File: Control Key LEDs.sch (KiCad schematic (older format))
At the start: 32 parts

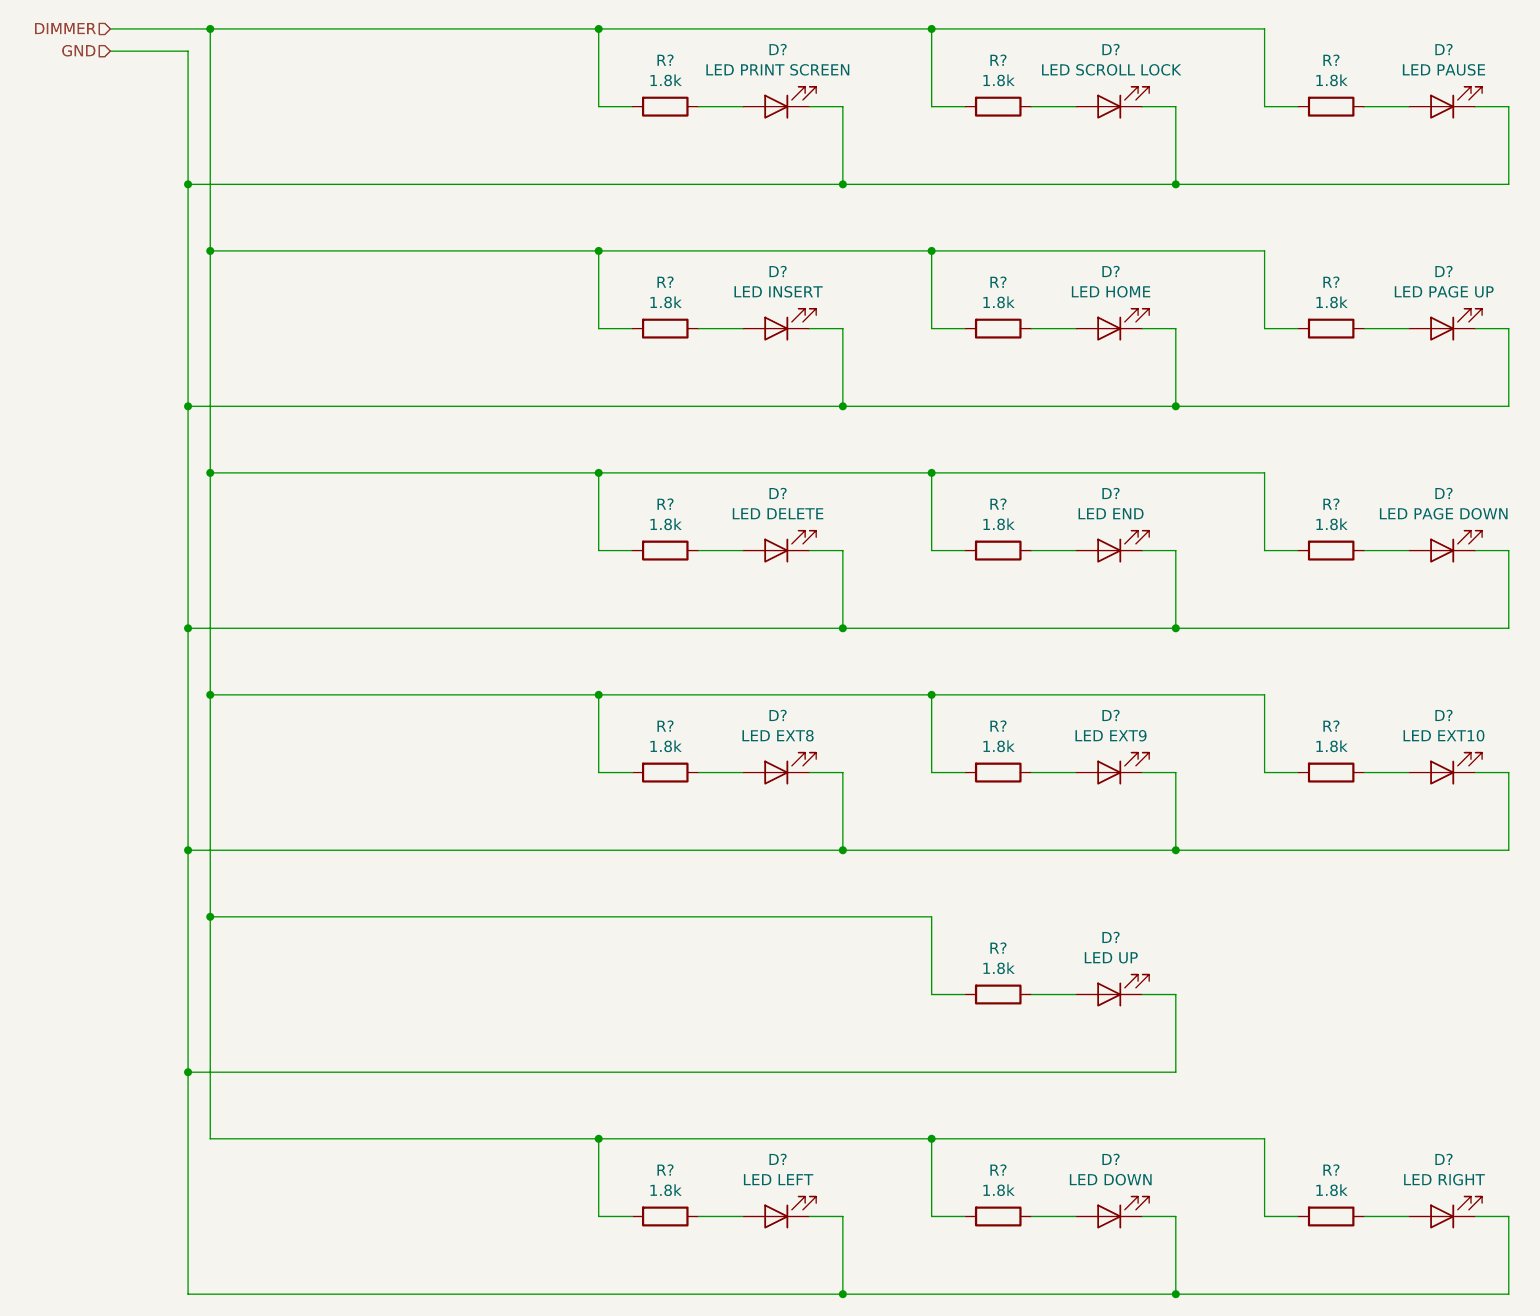
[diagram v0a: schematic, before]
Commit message: Corrected errors found in design rule check
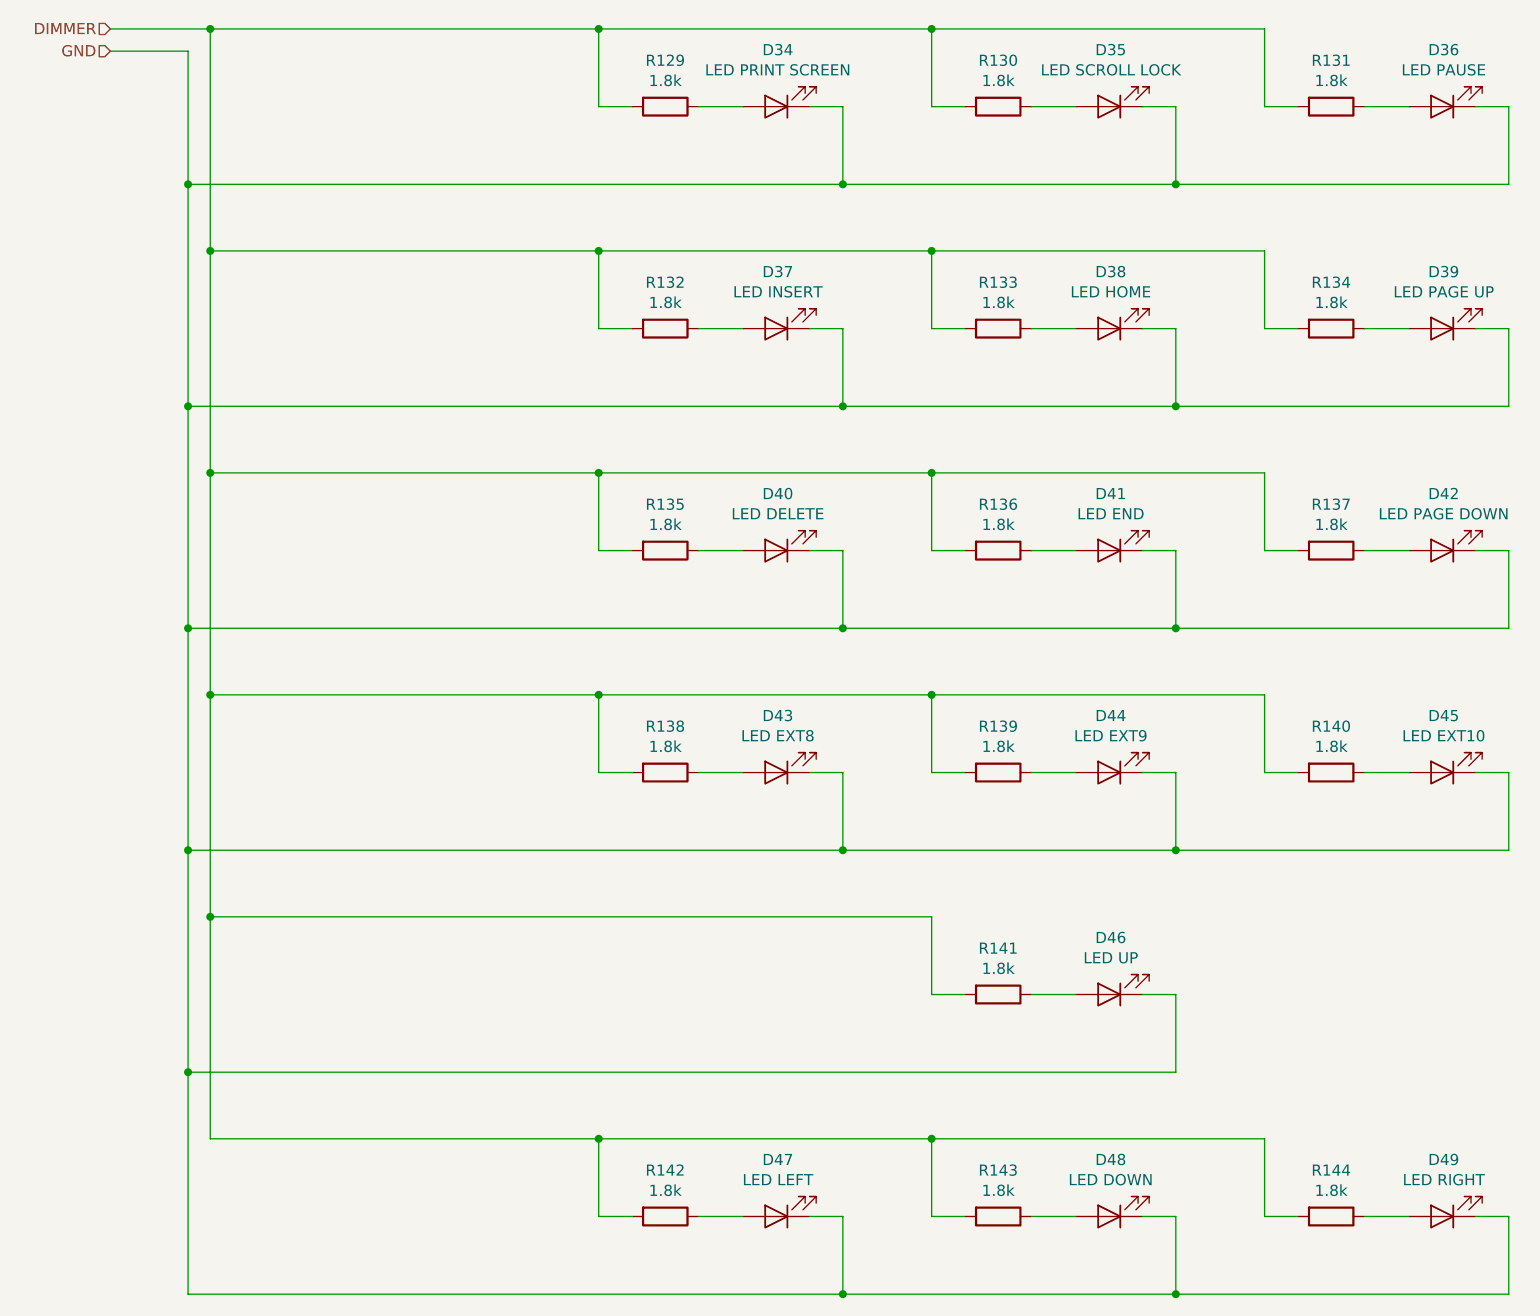
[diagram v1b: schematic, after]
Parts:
- D34, D35, D36, D37, D38, D39, D40, D41, D42, D43, D44, D45, D46, D47, D48, D49: renamed from D?; footprint (none) -> LED_SMD:LED_1206_3216Metric_ReverseMount_Hole1.8x2.4mm
- R129, R130, R131, R132, R133, R134, R135, R136, R137, R138, R139, R140, R141, R142, R143, R144: renamed from R?; footprint (none) -> Resistor_SMD:R_1206_3216Metric_Pad1.42x1.75mm_HandSolder

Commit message: Redesigned for single large PCB
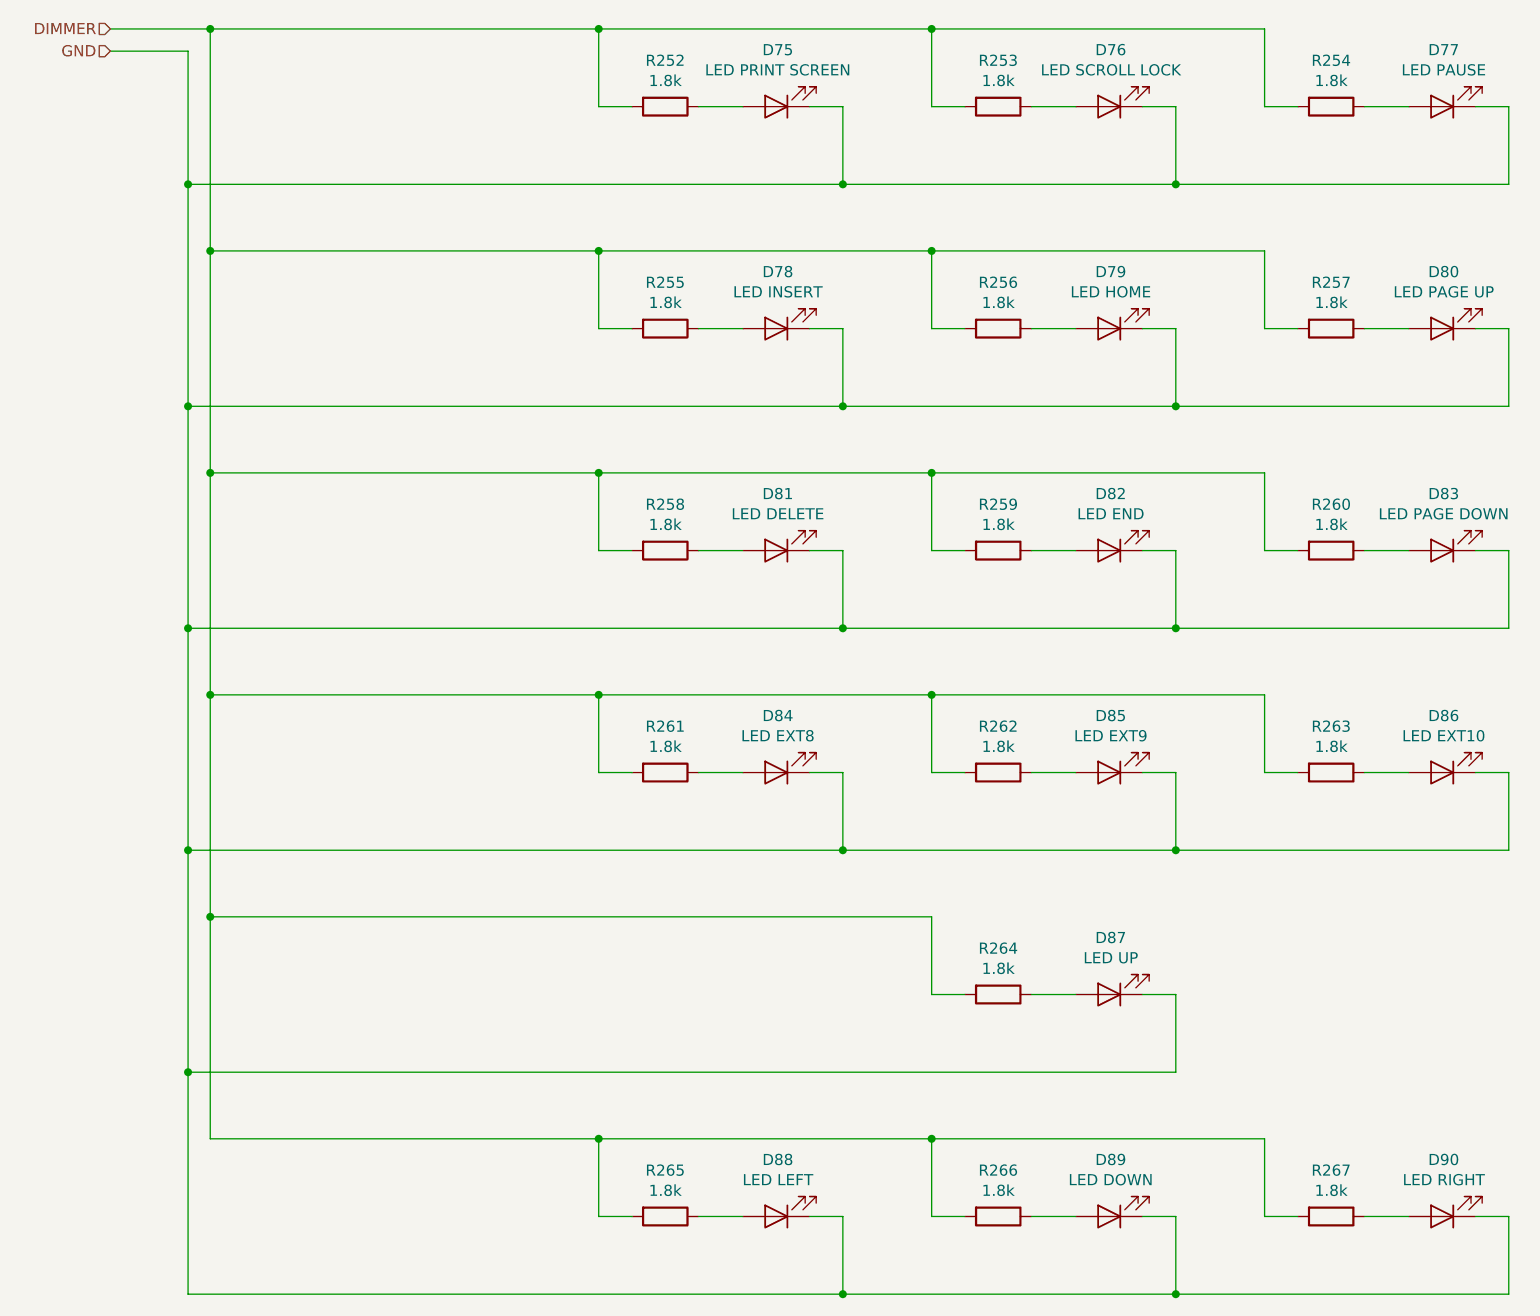
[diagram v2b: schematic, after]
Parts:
- renumbered D34 to D75, D35 to D76, D36 to D77, D37 to D78, D38 to D79, D39 to D80, D40 to D81, D41 to D82, D42 to D83, D43 to D84, D44 to D85, D45 to D86, D46 to D87, D47 to D88, D48 to D89, D49 to D90, R129 to R252, R130 to R253, R131 to R254, R132 to R255, R133 to R256, R134 to R257, R135 to R258, R136 to R259, R137 to R260, R138 to R261, R139 to R262, R140 to R263, R141 to R264, R142 to R265, R143 to R266, R144 to R267
